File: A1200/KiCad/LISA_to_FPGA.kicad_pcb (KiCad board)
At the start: 4 copper layers, 54.9 x 37 mm, 16 parts, among them J1 Conn_01x03, J2 Conn_01x40, U1 LM1117-3.3, U2 74LVC245A, U3 74LVC245A, U4 74LVC245A, U5 74LVC245A, U6 LISA

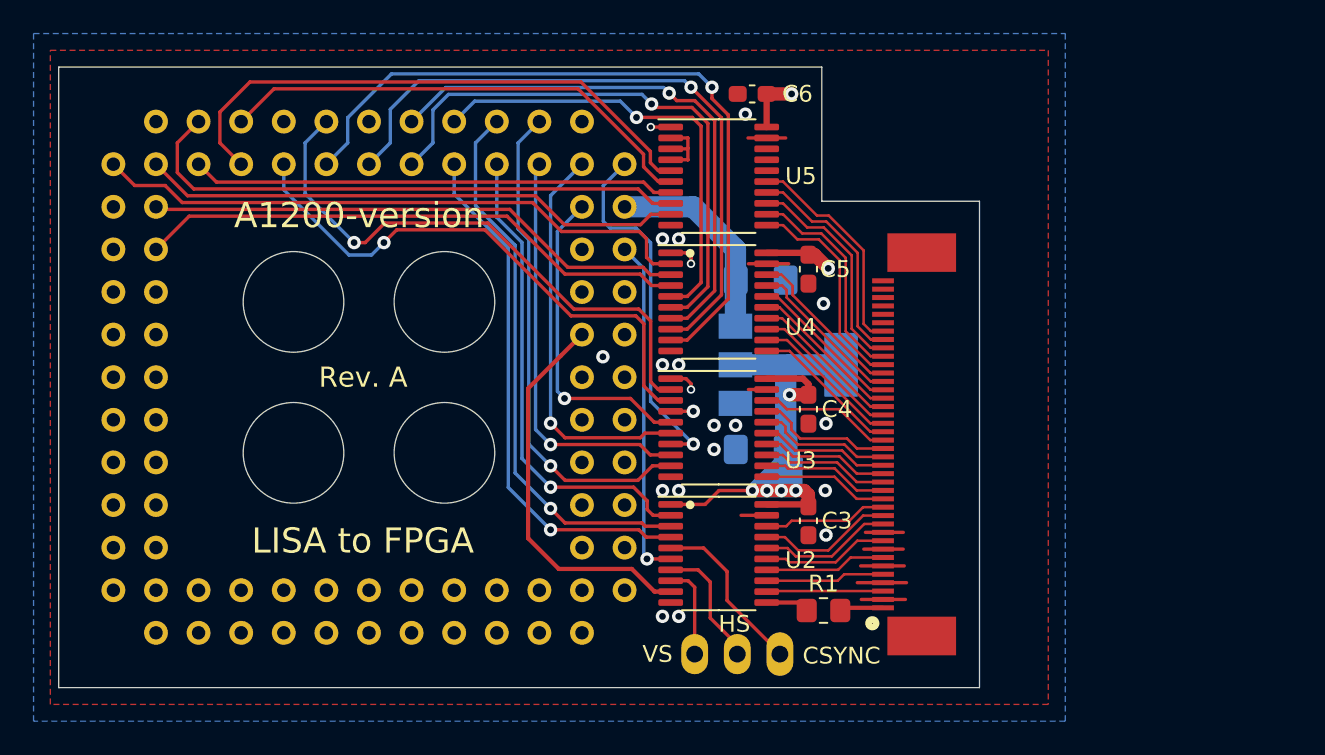
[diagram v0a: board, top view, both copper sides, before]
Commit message: Redesign of adapter on a 2-layer PCB, changed to 74LVC16244ADGG level shifters, changed sampling clock to C28OUT now sent to the FPGA
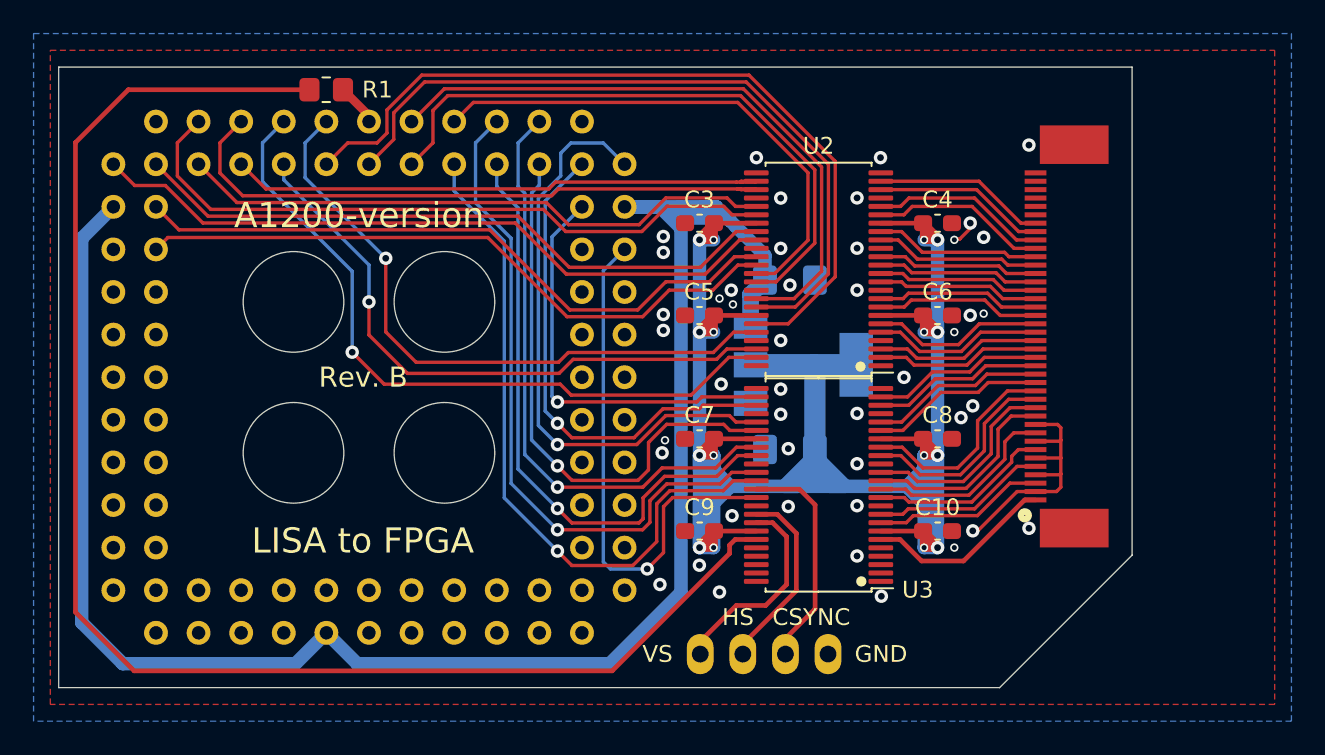
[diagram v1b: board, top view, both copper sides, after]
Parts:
- removed the U4 at (187.6, 85.9)
- removed U5: 74LVC245A, Package_SO:TSSOP-20_4.4x6.5mm_P0.65mm
- added C10: 0.1uF, Capacitor_SMD:C_0603_1608Metric_Pad1.08x0.95mm_HandSolder, F.Cu at (200.7, 99.6)
- added C7: 0.1uF, Capacitor_SMD:C_0603_1608Metric_Pad1.08x0.95mm_HandSolder, F.Cu at (186.5, 94.1)
- added C8: 0.1uF, Capacitor_SMD:C_0603_1608Metric_Pad1.08x0.95mm_HandSolder, F.Cu at (200.7, 94.1)
- added C9: 0.1uF, Capacitor_SMD:C_0603_1608Metric_Pad1.08x0.95mm_HandSolder, F.Cu at (186.5, 99.6)
- J1: value Conn_01x03 -> Conn_01x04; footprint Connector_PinHeader_2.54mm:PinHeader_1x03_P2.54mm_Horizontal -> Connector_PinHeader_2.54mm:PinHeader_1x04_P2.54mm_Horizontal
- R1: value 33 Ω -> 33Ω
- U2, U3: value 74LVC245A -> 74LVC16244ADGG; footprint Package_SO:TSSOP-20_4.4x6.5mm_P0.65mm -> Package_SO:TSSOP-48_6.1x12.5mm_P0.5mm
- moved R1 42.9 mm to (164.2, 73.3), turned to 0 degrees
- moved REF** 22.9 mm to (206.5, 76.8)
- moved C3 18.9 mm to (186.5, 81.2), turned to 0 degrees
- moved U2 18.0 mm to (193.6, 84.0), turned to 180 degrees
- moved C6 17.2 mm to (200.7, 86.7), turned to 180 degrees
- moved C4 13.5 mm to (200.7, 81.2), turned to 180 degrees
- moved J2 11.1 mm to (208.4, 88.0)
- moved C5 7.05 mm to (186.5, 86.7), turned to 0 degrees
- moved U3 6.86 mm to (193.6, 96.8), turned to 180 degrees
- moved J1 2.87 mm to (194.1, 106.9)
- moved C1 1.74 mm to (191.9, 84.6)
- moved C2 1.74 mm to (191.9, 94.7)
- moved U1 0.90 mm to (192.7, 89.7)
- renumbered U6 to U4
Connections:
- J1 pad 1: CSYNC -> GND
- J1 pad 2: HSYNC -> CSYNC
- J1 pad 3: VSYNC -> HSYNC
- J2 pad 1: /C14M_3V3 -> C28O_3V3
- R1 pad 1: /C14M_3V3 -> Net-(R1-Pad1)
- R1 pad 2: C14OUT_3V3 -> C28O
- U2 pad 1: 3V3 -> GND
- U2 pad 11: C14OUT_3V3 -> G1_3V3
- U2 pad 12: VSYNC_3V3 -> G0_3V3
- U2 pad 13: HSYNC_3V3 -> R7_3V3
- U2 pad 14: PIXELSW_3V3 -> R6_3V3
- U2 pad 15: CSYNC_3V3 -> GND
- U2 pad 16: B7_3V3 -> R5_3V3
- U2 pad 17: B6_3V3 -> R4_3V3
- U2 pad 18: B5_3V3 -> 3V3
- U2 pad 19: GND -> R3_3V3
- U2 pad 2: B5 -> G7_3V3
- U2 pad 20: 3V3 -> R2_3V3
- U2 pad 3: B6 -> G6_3V3
- U2 pad 4: B7 -> GND
- U2 pad 5: CSYNC -> G5_3V3
- U2 pad 6: PIXELSW -> G4_3V3
- U2 pad 7: HSYNC -> 3V3
- U2 pad 8: VSYNC -> G3_3V3
- U2 pad 9: C14OUT -> G2_3V3
- U3 pad 1: 3V3 -> GND
- U3 pad 11: B4_3V3 -> PIXELSW_3V3
- U3 pad 12: B3_3V3 -> CSYNC_3V3
- U3 pad 13: B2_3V3 -> B7_3V3
- U3 pad 14: B1_3V3 -> B6_3V3
- U3 pad 15: B0_3V3 -> GND
- U3 pad 16: G7_3V3 -> B5_3V3
- U3 pad 17: G6_3V3 -> B4_3V3
- U3 pad 18: G5_3V3 -> 3V3
- U3 pad 19: GND -> B3_3V3
- U3 pad 2: G5 -> Net-(U3-Pad2)
- U3 pad 20: 3V3 -> B2_3V3
- U3 pad 3: G6 -> Net-(U3-Pad3)
- U3 pad 4: G7 -> GND
- U3 pad 5: B0 -> Net-(U3-Pad5)
- U3 pad 6: B1 -> C28O_3V3
- U3 pad 7: B2 -> 3V3
- U3 pad 8: B3 -> VSYNC_3V3
- U3 pad 9: B4 -> HSYNC_3V3
- U4 pad 23: C14OUT -> Net-(U4-Pad23)
- U4 pad 43: Net-(U6-Pad43) -> C28O
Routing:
- net 3V3: track 54.0 -> 180.2 mm, vias 10 -> 16
- net Net-(R1-Pad1): track 0.00 -> 88.8 mm
- net VCC: track 69.7 -> 111.7 mm
- net C14OUT: track 23.3 -> 0.00 mm
- net B2: track 21.7 -> 35.7 mm
- net PIXELSW: track 20.4 -> 31.8 mm
- net C28O_3V3: track 0.00 -> 11.3 mm
- net B7: track 31.5 -> 41.2 mm
- net B3: track 24.6 -> 33.5 mm
- net R1: track 29.1 -> 37.6 mm
- net B5: track 28.7 -> 36.6 mm
- net B6: track 33.0 -> 40.9 mm
- net R6: track 32.4 -> 39.7 mm
- net VSYNC: track 5.58 -> 12.6 mm
- net R4: track 32.4 -> 39.2 mm
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- removed copper zone on 3V3.Cu, net 3V3
- removed copper zone on GND.Cu, net GND
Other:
- board size 54.9 x 37 mm -> 64 x 37 mm
- copper layers 4 -> 2
- board text added: "Design by J.Bilander (C) 2023, 2024"
- board text added: "GND"
- board text added: "Rev. B"
- board text removed: "Design by J.Bilander (C) 2023"
- board text removed: "Rev. A"
